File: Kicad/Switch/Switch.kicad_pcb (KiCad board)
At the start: 2 copper layers, 63.5 x 53.3 mm, 15 parts, among them Q1 BD139, Q2 IXTH90P10P, Q4 BD139, Q5A1 BSC340N08NS3G, Q6 BD139

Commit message: update sockets
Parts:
- added J1: Conn_01x01_Socket, Connector_PinSocket_1.27mm:PinSocket_1x01_P1.27mm_Vertical, F.Cu at (124.5, 58.4)
- added J2: Conn_01x01_Socket, Connector_PinSocket_1.27mm:PinSocket_1x01_P1.27mm_Vertical, F.Cu at (124.5, 73.7)
- added J3: Conn_01x01_Socket, Connector_PinSocket_1.27mm:PinSocket_1x01_P1.27mm_Vertical, F.Cu at (165.1, 58.4)
- turned Q5A1 to 180 degrees
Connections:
- Q1 pad 2: +1V0 -> Net-(J1-Pin_1)
- Q2 pad 1: +1V0 -> Net-(J1-Pin_1)
- Q4 pad 3: +1V0 -> Net-(J2-Pin_1)
- R2 pad 1: +1V0 -> Net-(J1-Pin_1)
- R25 pad 2: +1V0 -> Net-(J2-Pin_1)
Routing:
- net +1V0: track 74.2 -> 0.00 mm
- net GND: track 0.00 -> 58.7 mm
- net Net-(J1-Pin_1): track 0.00 -> 53.1 mm
- net Net-(J2-Pin_1): track 0.00 -> 33.7 mm
- net Net-(D2-K): track 53.0 -> 70.1 mm
- net Net-(J3-Pin_1): track 48.1 -> 53.0 mm

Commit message: update ground plate
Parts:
- renumbered J1 to V56, J2 to VTackt1, J3 to Vout1
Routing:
- net GND: track 58.7 -> 0.00 mm
- net Net-(C19-Pad1): track 6.28 -> 7.19 mm
- added copper zone on B.Cu, net GND
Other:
- board size 63.5 x 53.3 mm -> 68.6 x 55.9 mm

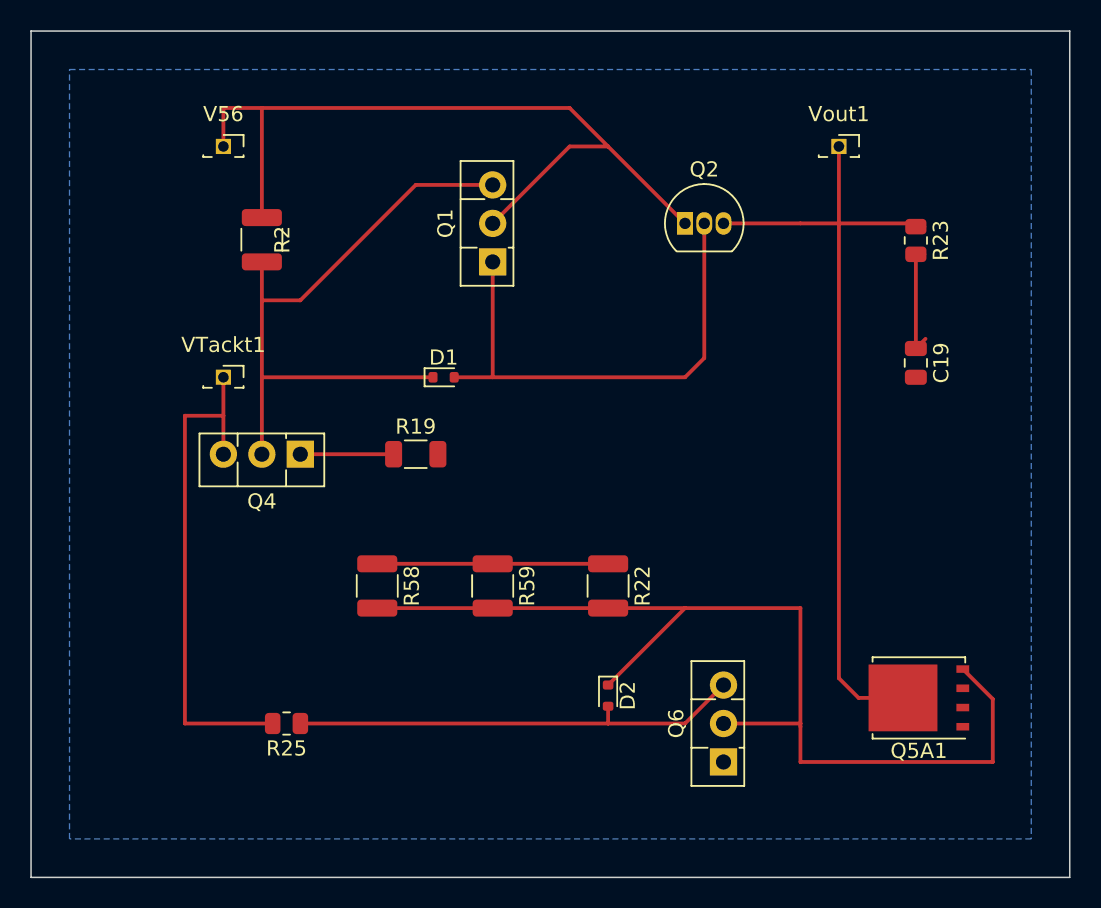
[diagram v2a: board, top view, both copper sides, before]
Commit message: Ground plate connected
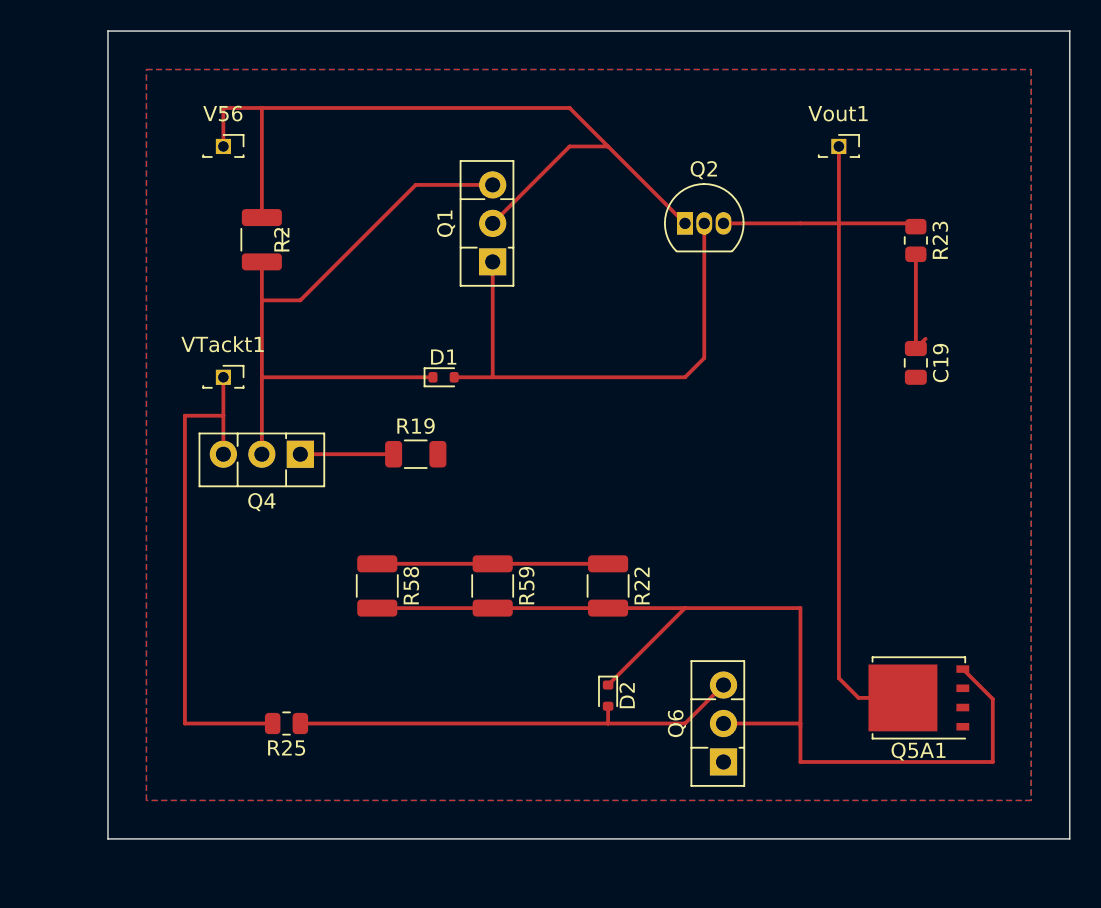
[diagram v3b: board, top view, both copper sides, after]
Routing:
- added copper zone on F.Cu, net GND
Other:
- board size 68.6 x 55.9 mm -> 63.5 x 53.3 mm
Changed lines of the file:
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@@
   (gr_poly
     (pts
-      (xy 111.76 50.8)
+      (xy 116.84 50.8)
       (xy 180.34 50.8)
-      (xy 180.34 106.68)
-      (xy 111.76 106.68)
+      (xy 180.34 104.14)
+      (xy 116.84 104.14)
     )
     (stroke (width 0.1) (type solid)) (fill none) (layer "Edge.Cuts"))
@@
   (segment (start 124.46 76.2) (end 124.46 78.74) (width 0.25) (layer "F.Cu") (net 11))
   (segment (start 124.46 76.2) (end 121.92 76.2) (width 0.25) (layer "F.Cu") (net 11))
-  (zone (net 2) (net_name "GND") (layer "B.Cu") (hatch edge 0.5)
+  (zone (net 2) (net_name "GND") (layers "F&B.Cu") (hatch edge 0.5)
     (connect_pads (clearance 0.5))
     (min_thickness 0.25) (filled_areas_thickness no)
@@
     (polygon
       (pts
-        (xy 114.3 53.34)
+        (xy 119.38 53.34)
         (xy 177.8 53.34)
-        (xy 177.8 104.14)
-        (xy 114.3 104.14)
+        (xy 177.8 101.6)
+        (xy 119.38 101.6)
       )
     )
